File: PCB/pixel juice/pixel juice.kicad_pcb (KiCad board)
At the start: 2 copper layers, 99.7 x 49.3 mm, 39 parts, among them J1 n8 Bus Connector, J2 Conn_01x03_Male, J3 PJRAN3X1U03X, U1 TMS9128, U2 TMS4416, U3 TMS4416, U4 74LS32, U5 LM1881, U6 4066, U7 AD8054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

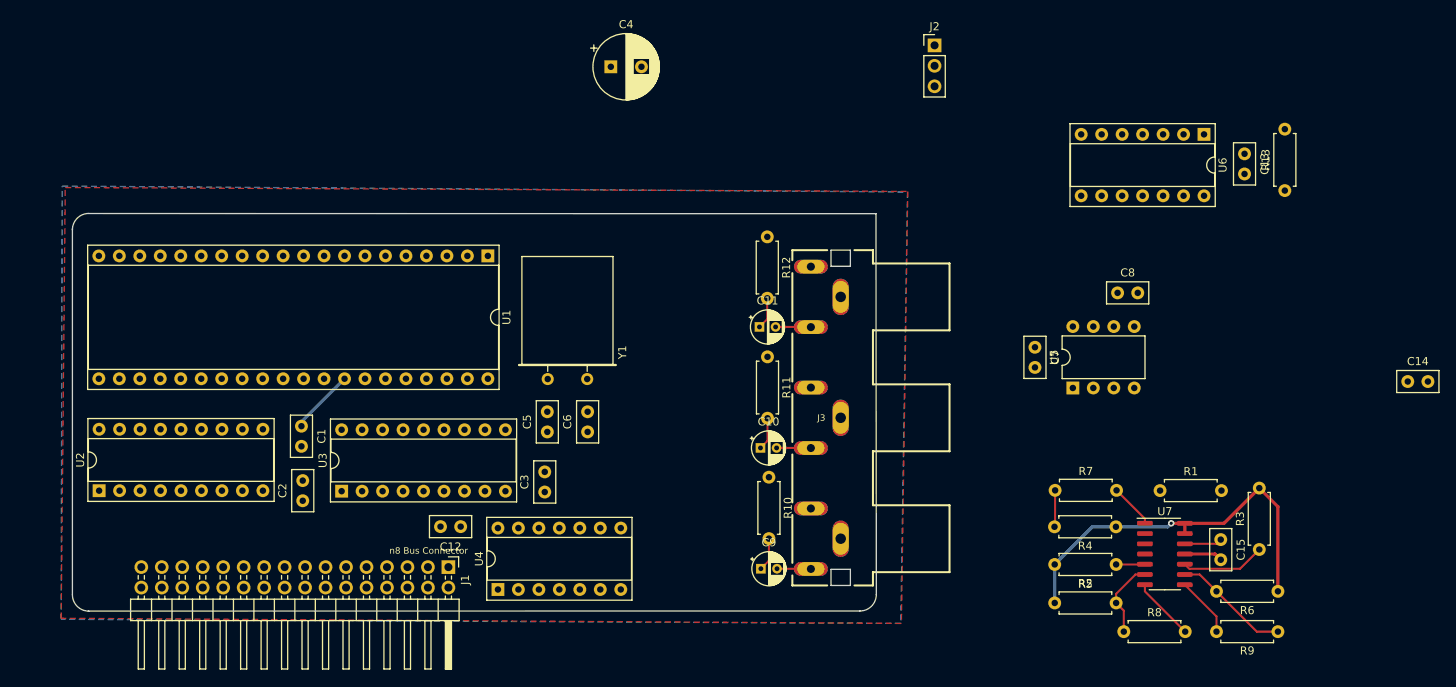
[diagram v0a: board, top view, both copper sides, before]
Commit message: horizontal layout for vram but i want to try vertical
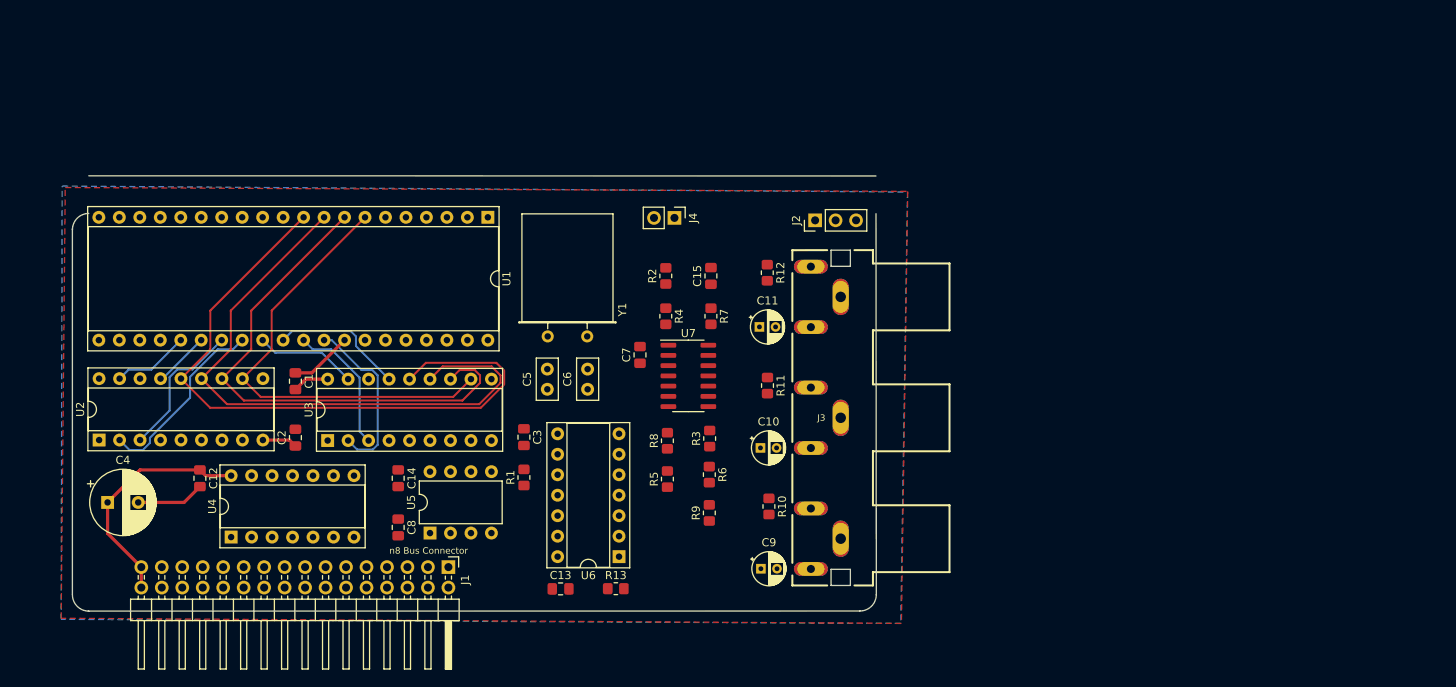
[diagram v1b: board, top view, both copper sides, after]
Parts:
- added J4: AUDIO_CLK, Connector_PinHeader_2.54mm:PinHeader_1x02_P2.54mm_Vertical, F.Cu at (175.3, 69.2)
- C1, C12, C13, C14, C15, C2, C3, C7, C8: footprint Capacitor_THT:C_Disc_D5.0mm_W2.5mm_P2.50mm -> Capacitor_SMD:C_0805_2012Metric_Pad1.18x1.45mm_HandSolder
- J2: value Conn_01x03_Male -> IRQ_SEL
- R1, R10, R11, R12, R13, R2, R3, R4, R5, R6, R7, R8, R9: footprint Resistor_THT:R_Axial_DIN0207_L6.3mm_D2.5mm_P7.62mm_Horizontal -> Resistor_SMD:R_0805_2012Metric_Pad1.20x1.40mm_HandSolder
- moved C14 125.8 mm to (141.0, 101.5), turned to -90 degrees
- moved C13 100.6 mm to (161.2, 115.2), turned to 0 degrees
- moved R13 96.6 mm to (168.0, 115.2), turned to 0 degrees
- moved C8 93.9 mm to (141.0, 107.6), turned to -90 degrees
- moved U6 89.5 mm to (168.4, 111.2), turned to 180 degrees
- moved C4 82.6 mm to (104.9, 104.5)
- moved U5 81.8 mm to (144.9, 108.3)
- moved R1 78.9 mm to (156.6, 101.4), turned to 90 degrees
- moved R9 72.1 mm to (179.6, 105.8), turned to 90 degrees
- moved R6 72.0 mm to (179.6, 101.0), turned to -90 degrees
- moved C15 71.2 mm to (179.8, 76.4), turned to 90 degrees
- moved R3 69.6 mm to (179.6, 96.6)
- moved R2 66.4 mm to (174.2, 76.4), turned to 90 degrees
- moved U7 63.1 mm to (177.0, 88.8)
- moved R4 61.7 mm to (174.2, 81.4), turned to -90 degrees
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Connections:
- J1 pad 6: unconnected-(J1-Pad6) -> AUDIO_CLK_{OUT}
- U1 pad 37: unconnected-(U1-Pad37) -> AUDIO_CLK_{IN}
- U4 pad 10: (no net) -> GND
- U4 pad 11: (no net) -> unconnected-(U4-Pad11)
- U4 pad 12: (no net) -> GND
- U4 pad 13: (no net) -> GND
- U4 pad 8: (no net) -> unconnected-(U4-Pad8)
- U4 pad 9: (no net) -> GND
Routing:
- net Net-(U1-Pad10): track 0.00 -> 83.8 mm
- net Net-(U1-Pad9): track 0.00 -> 76.6 mm
- net Net-(U1-Pad8): track 0.00 -> 65.7 mm
- net Net-(U1-Pad7): track 0.00 -> 56.5 mm
- net VREF: track 49.1 -> 0.00 mm, vias 1 -> 0
- net +5V: track 8.64 -> 41.7 mm
- net RD4: track 0.00 -> 23.3 mm
- net RD0: track 0.00 -> 21.4 mm
- net RD5: track 0.00 -> 17.7 mm
- net RD1: track 0.00 -> 17.1 mm
- net RD2: track 0.00 -> 16.8 mm
- net Net-(R9-Pad1): track 14.5 -> 0.00 mm
- net RD3: track 0.00 -> 12.6 mm
- net Net-(U6-Pad3): track 10.5 -> 0.00 mm
- net Net-(R5-Pad2): track 9.65 -> 0.00 mm
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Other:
- board size 99.7 x 49.3 mm -> 99.7 x 54 mm

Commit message: Video card + bus driver changes
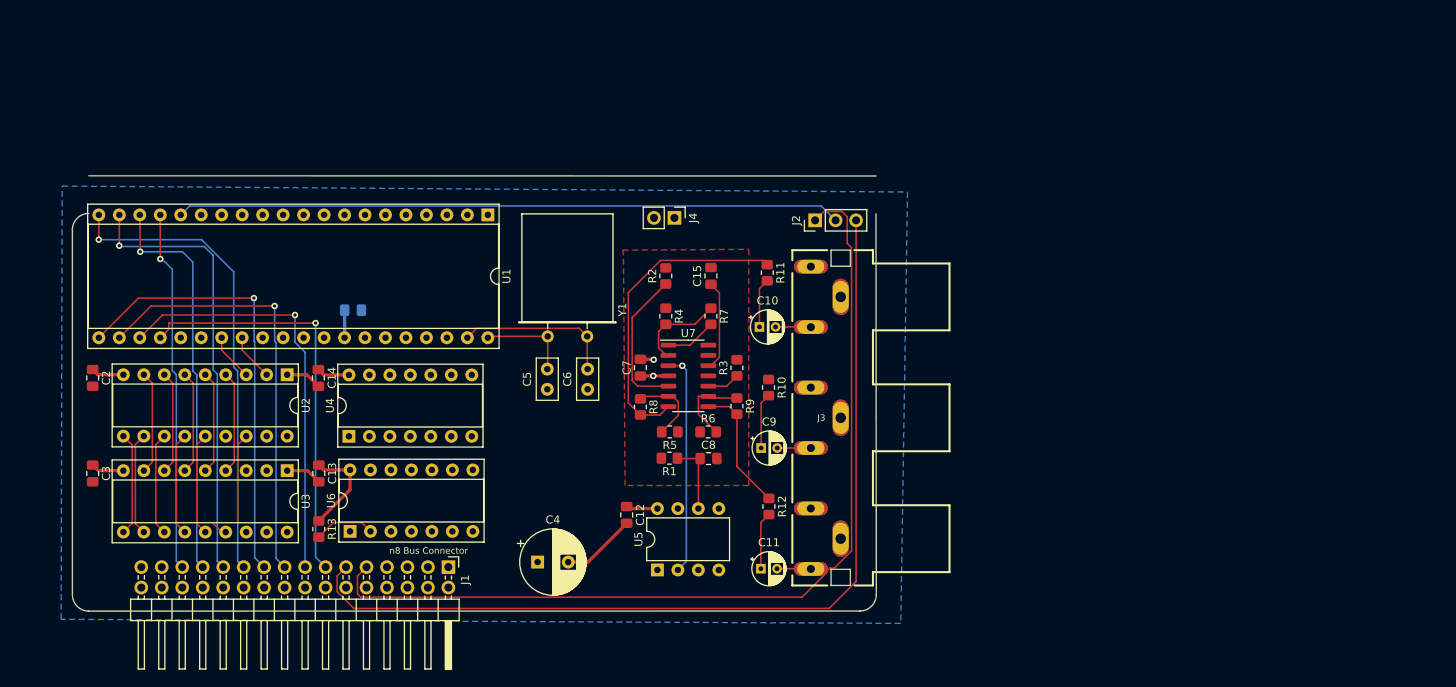
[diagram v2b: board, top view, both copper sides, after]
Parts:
- C1: moved to B.Cu
- moved C4 53.9 mm to (158.3, 111.9)
- moved C3 53.7 mm to (103.1, 100.9)
- moved C12 53.1 mm to (169.3, 106.0)
- moved C8 39.4 mm to (179.5, 99.1), turned to 0 degrees
- moved R13 37.6 mm to (131.2, 107.8), turned to -90 degrees
- moved U6 33.5 mm to (135.0, 108.1), turned to 90 degrees
- moved C13 33.2 mm to (131.2, 100.9), turned to -90 degrees
- moved C11 30.0 mm to (186.0, 112.7)
- moved R12 29.0 mm to (187.0, 105.0)
- moved U5 28.6 mm to (173.2, 112.9)
- moved C2 26.2 mm to (103.1, 89.0), turned to -90 degrees
- moved U2 24.7 mm to (127.2, 88.7), turned to -90 degrees
- moved U4 19.2 mm to (134.9, 96.3)
- moved R1 18.2 mm to (174.7, 99.0), turned to 180 degrees
- moved C14 15.9 mm to (131.1, 89.0)
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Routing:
- net ~{IRQ}: track 0.00 -> 114.9 mm
- net ~{NMI}: track 0.00 -> 114.1 mm
- net ~{INT}: track 0.00 -> 82.4 mm
- net Net-(U1-Pad10): track 83.8 -> 12.8 mm
- net Net-(U1-Pad9): track 76.6 -> 12.8 mm
- net D3: track 0.00 -> 58.6 mm, vias 0 -> 1
- net D4: track 0.00 -> 55.2 mm, vias 0 -> 1
- net D2: track 0.00 -> 55.2 mm, vias 0 -> 1
- net D5: track 0.00 -> 53.8 mm, vias 0 -> 1
- net Net-(U1-Pad8): track 65.7 -> 12.8 mm
- net D6: track 0.00 -> 52.2 mm, vias 0 -> 1
- net D7: track 0.00 -> 51.2 mm, vias 0 -> 1
- net D1: track 0.00 -> 50.0 mm, vias 0 -> 1
- net D0: track 0.00 -> 44.9 mm, vias 0 -> 1
- net Net-(U1-Pad7): track 56.5 -> 12.8 mm
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- added copper zone on In2.Cu, net +5V
- added copper zone on In1.Cu, net GND
- added copper zone on F.Cu, net VREF
- removed copper zone on F.Cu, net GND
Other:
- copper layers 2 -> 4

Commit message: Added amp stages
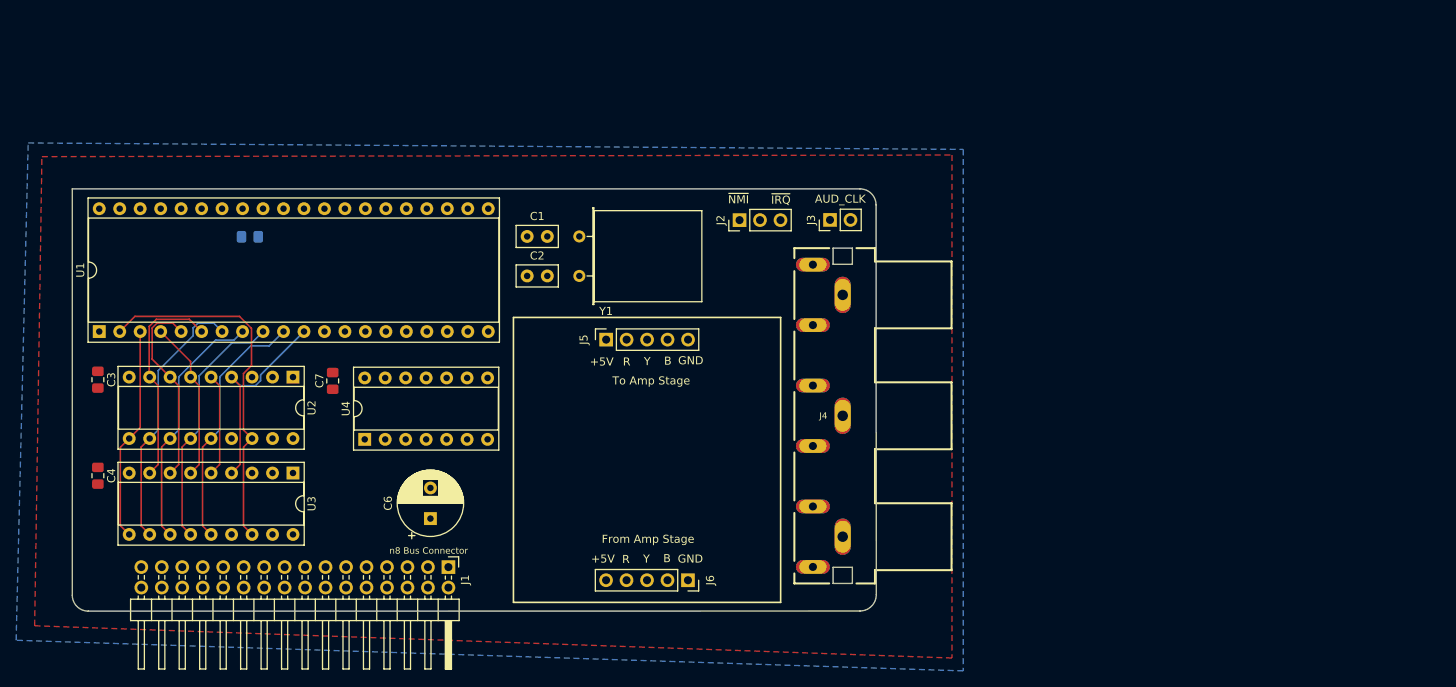
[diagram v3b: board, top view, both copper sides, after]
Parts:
- removed C10, C11, C9: 47uF, Capacitor_THT:CP_Radial_D4.0mm_P2.00mm
- removed C12, C13, C14: 100nF, Capacitor_SMD:C_0805_2012Metric_Pad1.18x1.45mm_HandSolder
- removed C15: 10nF, Capacitor_SMD:C_0805_2012Metric_Pad1.18x1.45mm_HandSolder
- removed C8: 100nf, Capacitor_SMD:C_0805_2012Metric_Pad1.18x1.45mm_HandSolder
- removed R1: 680k, Resistor_SMD:R_0805_2012Metric_Pad1.20x1.40mm_HandSolder
- removed R10, R11, R12: 75R, Resistor_SMD:R_0805_2012Metric_Pad1.20x1.40mm_HandSolder
- removed R13: 1K, Resistor_SMD:R_0805_2012Metric_Pad1.20x1.40mm_HandSolder
- removed R2, R3: 10k, Resistor_SMD:R_0805_2012Metric_Pad1.20x1.40mm_HandSolder
- removed R4, R5, R6: 2k, Resistor_SMD:R_0805_2012Metric_Pad1.20x1.40mm_HandSolder
- removed R7, R8, R9: 1k, Resistor_SMD:R_0805_2012Metric_Pad1.20x1.40mm_HandSolder
- removed U5: LM1881, Package_DIP:DIP-8_W7.62mm
- removed U6: 4066, Package_DIP:DIP-14_W7.62mm_Socket
- removed U7: AD8054, Package_SO:SOIC-14_3.9x8.7mm_P1.27mm
- added J5: TO_AMP, Connector_PinSocket_2.54mm:PinSocket_1x05_P2.54mm_Vertical, F.Cu at (166.8, 84.3)
- added J6: FROM_AMP, Connector_PinSocket_2.54mm:PinSocket_1x05_P2.54mm_Vertical, F.Cu at (176.9, 114.2)
- C1: value 100nF -> 22pf; footprint Capacitor_SMD:C_0805_2012Metric_Pad1.18x1.45mm_HandSolder -> Capacitor_THT:C_Disc_D5.0mm_W2.5mm_P2.50mm; moved to F.Cu
- C2: value 100nF -> 22pf; footprint Capacitor_SMD:C_0805_2012Metric_Pad1.18x1.45mm_HandSolder -> Capacitor_THT:C_Disc_D5.0mm_W2.5mm_P2.50mm
- C4: value 470uF -> 100nF; footprint Capacitor_THT:CP_Radial_D8.0mm_P3.80mm -> Capacitor_SMD:C_0805_2012Metric_Pad1.18x1.45mm_HandSolder
- C5: value 22pf -> 100nF; footprint Capacitor_THT:C_Disc_D5.0mm_W2.5mm_P2.50mm -> Capacitor_SMD:C_0805_2012Metric_Pad1.18x1.45mm_HandSolder; moved to B.Cu
- C6: value 22pf -> 470uF; footprint Capacitor_THT:C_Disc_D5.0mm_W2.5mm_P2.50mm -> Capacitor_THT:CP_Radial_D8.0mm_P3.80mm
- J3: value PJRAN3X1U03X -> AUDIO_CLK; footprint PJRAN3X1U03X:PJRAN3X1U01X -> Connector_PinHeader_2.54mm:PinHeader_1x02_P2.54mm_Vertical
- J4: value AUDIO_CLK -> PJRAN3X1U03X; footprint Connector_PinHeader_2.54mm:PinHeader_1x02_P2.54mm_Vertical -> PJRAN3X1U03X:PJRAN3X1U01X
- moved C4 55.6 mm to (103.7, 101.2), turned to -90 degrees
- moved C2 55.4 mm to (157.0, 76.4), turned to 0 degrees
- moved U1 50.3 mm to (103.9, 83.3), turned to 90 degrees
- moved C5 41.5 mm to (122.6, 71.5), turned to 0 degrees
- moved C7 38.2 mm to (132.9, 89.4), turned to -90 degrees
- moved J4 30.7 mm to (193.8, 93.8), turned to 180 degrees
- moved C6 25.3 mm to (145.0, 106.5)
- moved J3 24.6 mm to (194.6, 69.5), turned to 90 degrees
- moved C1 23.5 mm to (157.0, 71.5)
- moved C3 11.6 mm to (103.7, 89.3)
- moved J2 9.38 mm to (183.3, 69.5)
- moved Y1 7.56 mm to (163.5, 76.4), turned to 90 degrees
- moved U4 1.99 mm to (136.8, 96.7)
- moved U2 0.78 mm to (128.0, 89.0)
- moved U3 0.78 mm to (128.0, 100.8)
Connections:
- C1 pad 1: +5V -> GND
- C1 pad 2: GND -> Net-(C1-Pad2)
- C2 pad 1: +5V -> GND
- C2 pad 2: GND -> Net-(C2-Pad2)
- C5 pad 1: GND -> +5V
- C5 pad 2: Net-(C5-Pad2) -> GND
- C6 pad 1: GND -> +5V
- C6 pad 2: Net-(C6-Pad2) -> GND
- J3 pad 1: GND -> AUDIO_CLK_{OUT}
- J3 pad 2: /Pb_{out} -> AUDIO_CLK_{IN}
- J4 pad 1: AUDIO_CLK_{OUT} -> GND
- J4 pad 2: AUDIO_CLK_{IN} -> /B-Y_{out}
- U1 pad 39: Net-(C6-Pad2) -> Net-(C2-Pad2)
- U1 pad 40: Net-(C5-Pad2) -> Net-(C1-Pad2)
- Y1 pad 1: Net-(C6-Pad2) -> Net-(C2-Pad2)
- Y1 pad 2: Net-(C5-Pad2) -> Net-(C1-Pad2)
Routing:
- net ~{IRQ}: track 114.9 -> 0.00 mm
- net ~{NMI}: track 114.1 -> 0.00 mm
- net ~{INT}: track 82.4 -> 0.00 mm
- net D3: track 58.6 -> 0.00 mm, vias 1 -> 0
- net D4: track 55.2 -> 0.00 mm, vias 1 -> 0
- net D2: track 55.2 -> 0.00 mm, vias 1 -> 0
- net D5: track 53.8 -> 0.00 mm, vias 1 -> 0
- net D6: track 52.2 -> 0.00 mm, vias 1 -> 0
- net D7: track 51.2 -> 0.00 mm, vias 1 -> 0
- net D1: track 50.0 -> 0.00 mm, vias 1 -> 0
- net D0: track 44.9 -> 0.00 mm, vias 1 -> 0
- net Net-(R11-Pad1): track 38.8 -> 0.00 mm
- net +5V: track 35.1 -> 0.00 mm, vias 1 -> 0
- net ~{CAS}: track 11.3 -> 45.0 mm
- net Y: track 27.7 -> 0.00 mm, vias 1 -> 0
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- added copper zone on F.Cu, net GND
- removed copper zone on In2.Cu, net +5V
- removed copper zone on In1.Cu, net GND
- removed copper zone on F.Cu, net VREF
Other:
- board size 99.7 x 54 mm -> 99.7 x 52.4 mm
- copper layers 4 -> 2
- board text added: "+5V"
- board text added: "AUD_CLK"
- board text added: "B"
- board text added: "From Amp Stage"
- board text added: "GND"
- board text added: "R"
- board text added: "To Amp Stage"
- board text added: "Y"
- board text added: "~{IRQ}"
- board text added: "~{NMI}"

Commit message: rc1 before library swap test
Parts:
- moved J2 86.2 mm to (105.4, 106.4), turned to 180 degrees
- moved U1 50.6 mm to (152.2, 68.0), turned to -90 degrees
- moved C6 29.5 mm to (115.5, 105.6)
- moved C7 29.5 mm to (103.3, 88.5)
- moved U4 29.5 mm to (107.3, 95.8)
- moved C3 24.1 mm to (127.8, 88.4)
- moved C4 24.1 mm to (127.8, 100.3)
- moved U2 24.1 mm to (152.0, 88.1)
- moved U3 24.1 mm to (152.0, 100.0)
- moved C5 17.2 mm to (137.8, 79.5)
- moved J5 0.33 mm to (166.8, 84.0)
- moved J6 0.30 mm to (176.9, 114.5)
- moved J4 0.10 mm to (193.7, 93.8)
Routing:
- net ~{IRQ}: track 0.00 -> 77.7 mm
- net AUDIO_CLK_{OUT}: track 0.00 -> 72.3 mm
- net D3: track 0.00 -> 67.4 mm
- net ~{READ}: track 0.00 -> 63.9 mm
- net AUDIO_CLK_{IN}: track 0.00 -> 63.7 mm
- net ~{NMI}: track 0.00 -> 62.8 mm
- net RD3: track 0.00 -> 62.6 mm, vias 0 -> 1
- net D2: track 0.00 -> 60.1 mm
- net D1: track 0.00 -> 51.0 mm
- net A0: track 0.00 -> 50.7 mm, vias 0 -> 1
- net ~{INT}: track 0.00 -> 50.5 mm
- net ~{RES}: track 0.00 -> 50.5 mm, vias 0 -> 1
- net RD2: track 0.00 -> 47.6 mm, vias 0 -> 1
- net D0: track 0.00 -> 47.4 mm
- net ~{WRITE}: track 0.00 -> 42.2 mm, vias 0 -> 1
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- added copper zone on In2.Cu, net +5V
- added copper zone on In1.Cu, net GND
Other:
- board size 99.7 x 52.4 mm -> 99.7 x 52.7 mm
- copper layers 2 -> 4
- board text added: "Pixel Juice v1.0b, April 2023 by Nate Rivard"
